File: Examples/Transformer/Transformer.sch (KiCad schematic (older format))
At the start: 6 parts, among them U1 TRANSFO, U2 plot_v1, U3 plot_v1

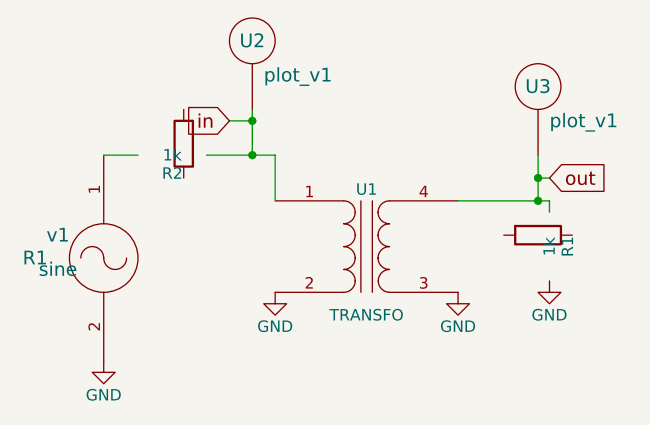
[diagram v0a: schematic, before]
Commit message: common code for Win and Linux, merged py2 changes
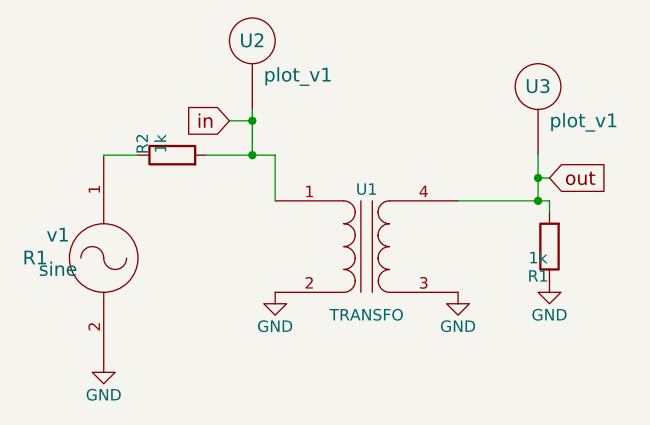
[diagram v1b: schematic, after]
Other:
- moved on the sheet: R1, R2
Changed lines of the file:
@@
 LIBS:74xx
 LIBS:cmos4000
-LIBS:test-cache
 EELAYER 25 0
 EELAYER END
@@
 L R R1
 U 1 1 56D6CC22
-P 5950 3750
-F 0 "R1" H 6000 3880 50  0000 C CNN
-F 1 "1k" H 6000 3800 50  0000 C CNN
-F 2 "" H 6000 3730 30  0000 C CNN
-F 3 "" V 6000 3800 30  0000 C CNN
-	1    5950 3750
-	0    1    1    0
+P 6000 3800
+F 0 "R1" H 6050 3930 50  0000 C CNN
+F 1 "1k" H 6050 3850 50  0000 C CNN
+F 2 "" H 6050 3780 30  0000 C CNN
+F 3 "" V 6050 3850 30  0000 C CNN
+	1    6000 3800
+	-1   0    0    1
 $EndComp
 $Comp
@@
 L R R2
 U 1 1 56D6D2F8
-P 4400 3350
-F 0 "R2" H 4450 3480 50  0000 C CNN
-F 1 "1k" H 4450 3400 50  0000 C CNN
-F 2 "" H 4450 3330 30  0000 C CNN
-F 3 "" V 4450 3400 30  0000 C CNN
-	1    4400 3350
-	-1   0    0    1
+P 4350 3400
+F 0 "R2" H 4400 3530 50  0000 C CNN
+F 1 "1k" H 4400 3450 50  0000 C CNN
+F 2 "" H 4400 3380 30  0000 C CNN
+F 3 "" V 4400 3450 30  0000 C CNN
+	1    4350 3400
+	0    -1   -1   0
 $EndComp
 Wire Wire Line
